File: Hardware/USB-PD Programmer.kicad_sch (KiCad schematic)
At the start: 22 parts, among them J1 Conn_01x08_Male, J2 Conn_01x04_Male, J3 Conn_01x02_Male, J4 Conn_01x02_Male, J5 Conn_01x02_Male, J6 Conn_01x02_Male, J7 Conn_01x07_Male, J9 QWIIC_Stackable, U1 R1501J033B-T1-JE, U2 CH340G, Y1 12M

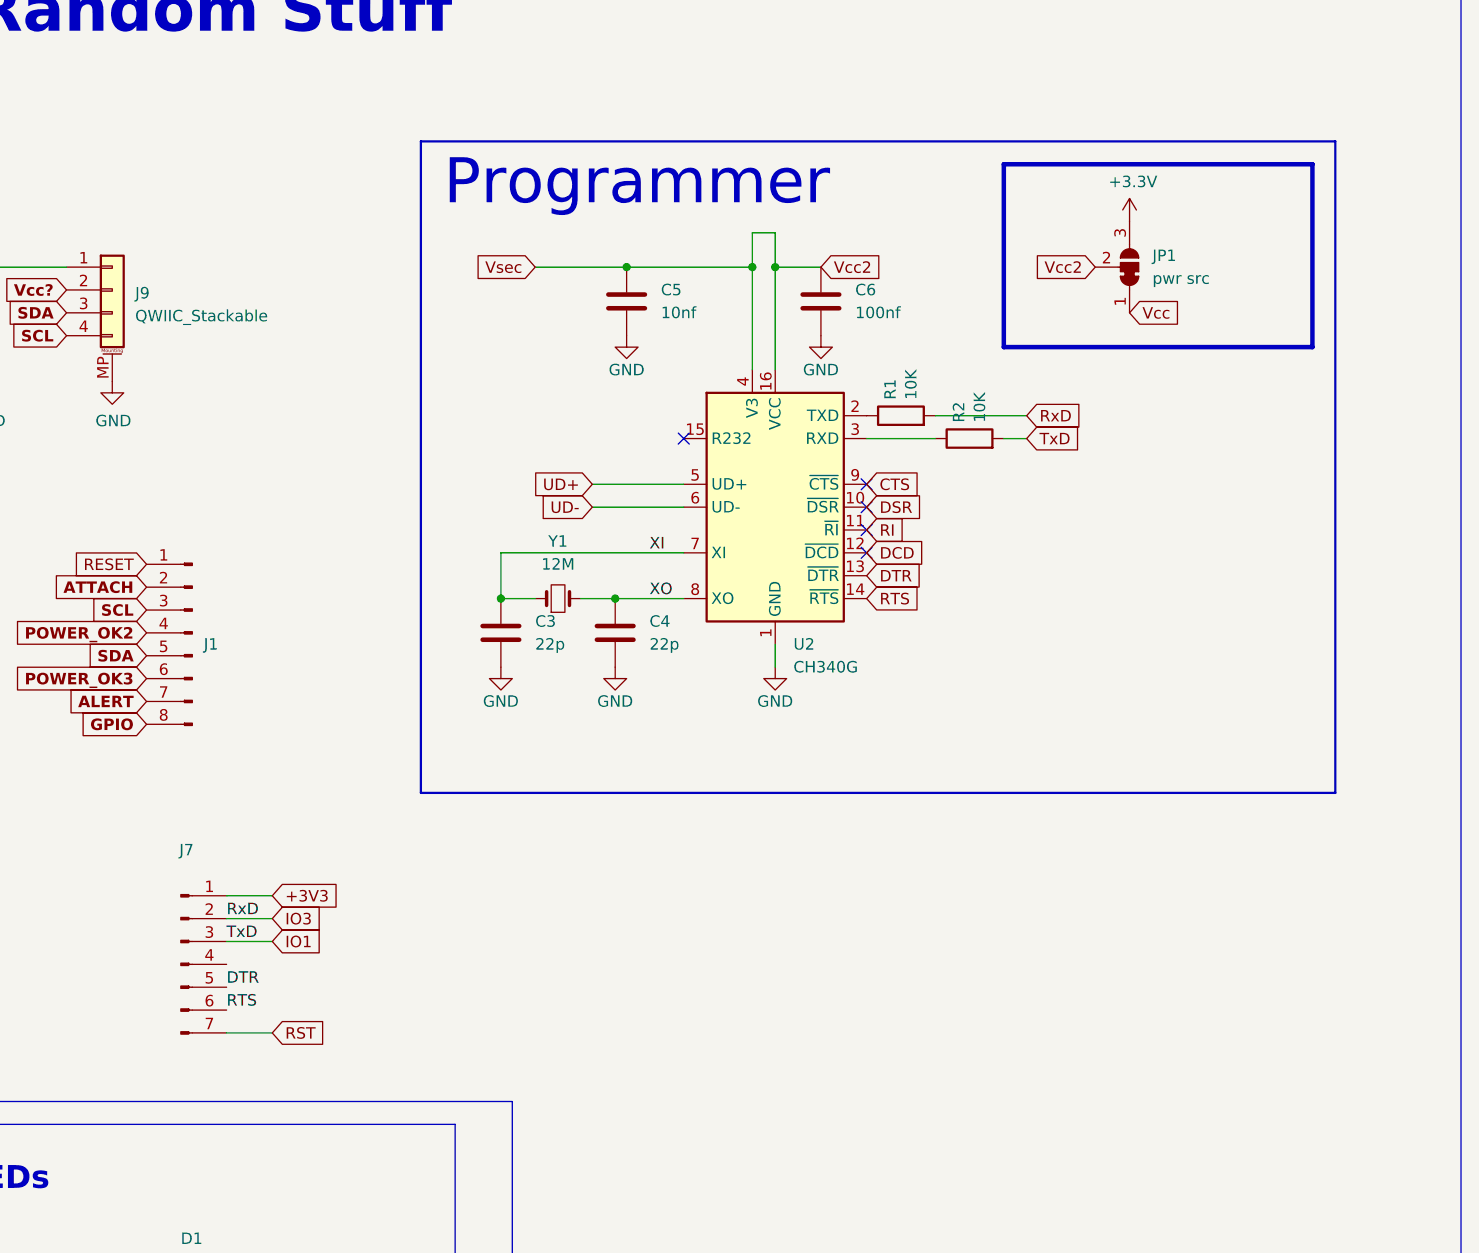
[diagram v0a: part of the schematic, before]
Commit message: Cleaned up design of the Programmer board
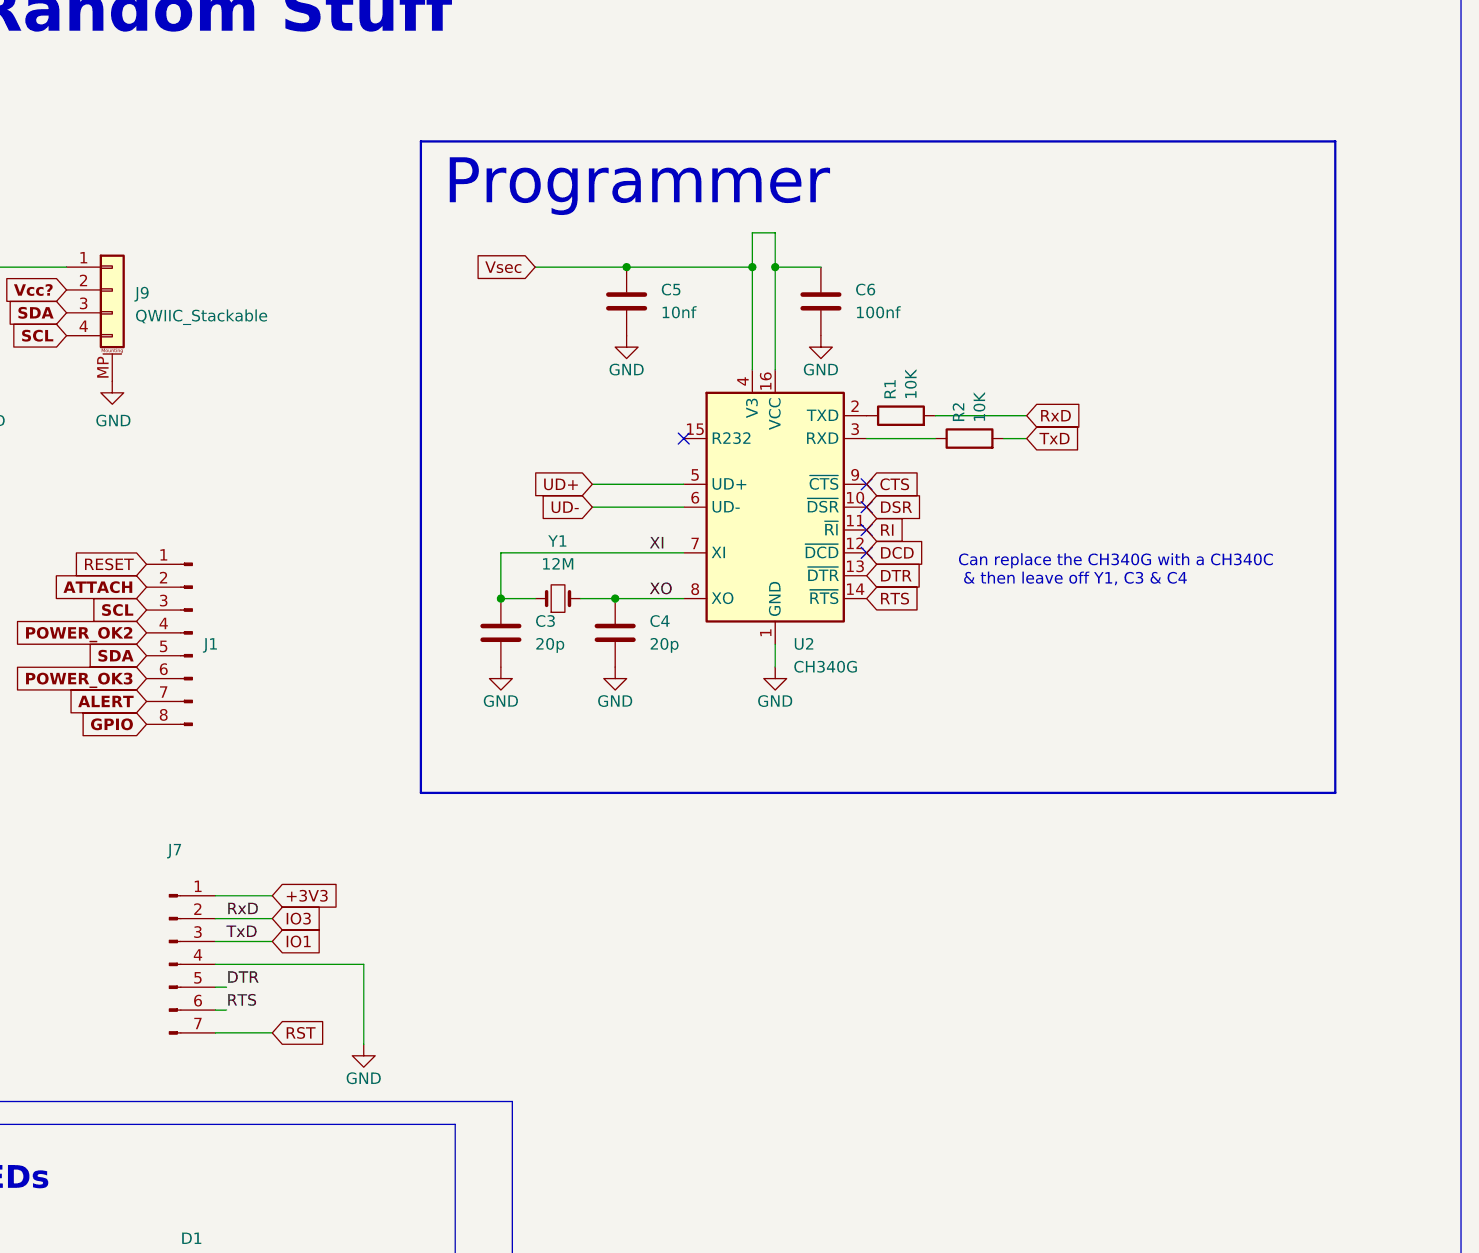
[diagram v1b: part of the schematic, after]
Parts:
- removed JP1: pwr src, Jumper:SolderJumper-3_P1.3mm_Bridged12_RoundedPad1.0x1.5mm_NumberLabels, symbol Jumper:SolderJumper_3_Bridged12
- C3, C4: value 22p -> 20p; LCSC C408549 (20pf C325469) -> C325469
- D1: footprint Footprints:SOT-23 (both sides) -> Package_TO_SOT_SMD:SOT-23
- R1, R2: LCSC (none) -> C25804
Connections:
- net GND: now also J7.4 (Pin_4)
- net Vcc2 renamed Vsec
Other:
- note added: "Can replace the CH340G with a CH340C & then leave off Y1, C3 & C4"
- moved on the sheet: J7

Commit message: Documentation...
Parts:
- added JP1: SolderJumper_2_Open, Tinker:SolderJumper-2_P_Open_Rounded_skinny, symbol Jumper:SolderJumper_2_Open
- U2: value CH340G -> CH340G/C; LCSC C14267 -> C14267/C84681
- renumbered J7 to J1, J1 to J7
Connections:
- net +3V3: now also JP1.2 (B)
- net Vsec: now also JP1.1 (A)
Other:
- moved on the sheet: J1

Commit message: Tinkerin' + RESET & LED on Programmer...
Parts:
- added D2: XL-2012RGBC, Tinker:XL-2012RGBC, symbol Device:LED_RGAB
- added D3: MHT170RGBCT, Tinker:MHT170RGBCT, symbol Device:LED_RGBA
- added R4, R5: 10K, Resistor_SMD:R_0603_1608Metric_Pad0.98x0.95mm_HandSolder, symbol Device:R
- added SW1: SW_Push, Tinker:SW_Push_TS273014TP, symbol Switch:SW_Push
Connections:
- net +3V3: now also SW1.2
- net GND: now also R4.1, R5.1
- net IO1: now also D2.1 (RK), D3.1 (RK)
- net IO3: now also D2.2 (GK), D3.2 (GK)
- net RST: now also SW1.1
- new net: D3.4 (A), R5.2
- new net: D2.3 (A), R4.2
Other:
- note added: "Board-Board"
- note added: "Control"
- note added: "QWIIC"
- moved on the sheet: C1, C2, J2, J3, J4, J5, J6, J7, J9, JP1, U1

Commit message: Programmer Board Indicators!
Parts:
- added D4: red, LED_SMD:LED_0603_1608Metric, symbol Device:LED
- added D5: green, LED_SMD:LED_0603_1608Metric, symbol Device:LED
- added D6, D7: yellow, LED_SMD:LED_0603_1608Metric, symbol Device:LED
- added R6, R7, R8, R9: 1k, Resistor_SMD:R_0603_1608Metric, symbol Device:R_US
- D2, R4: now left out of the parts list
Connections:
- net DTR: now also D6.1 (K)
- net GND: now also R6.1, R7.1
- net IO1: now also D4.2 (A)
- net IO3: now also D5.2 (A)
- net RTS: now also D7.1 (K)
- net Vsec: now also R8.2, R9.2
- new net: D6.2 (A), R8.1
- new net: D4.1 (K), R6.2
- new net: D5.1 (K), R7.2
- new net: D7.2 (A), R9.1
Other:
- moved on the sheet: D1, R3

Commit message: possibly, maybe, finalised Programmer Board?
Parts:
- removed D1: LED_Dual_AAK, Package_TO_SOT_SMD:SOT-23, symbol Device:LED_Dual_AAK
- removed D2: XL-2012RGBC, Tinker:XL-2012RGBC, symbol Device:LED_RGAB
- removed D3: MHT170RGBCT, Tinker:MHT170RGBCT, symbol Device:LED_RGBA
- removed R3, R4, R5: 10K, Resistor_SMD:R_0603_1608Metric_Pad0.98x0.95mm_HandSolder, symbol Device:R
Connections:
- net +3V3: no longer SW1.2
- net Vsec: now also SW1.2
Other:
- note removed: "grn"
- note removed: "red"
- title: Prototype Board -> USB-PD Programmer
- moved on the sheet: SW1

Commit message: Rabbit OCD attack...
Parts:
- added D1: blue, LED_SMD:LED_0603_1608Metric, symbol Device:LED
- added R1: 1k, Resistor_SMD:R_0603_1608Metric, symbol Device:R_US
- renumbered D4 to D2, D5 to D3, D6 to D4, D7 to D5, R6 to R2, R7 to R3, R8 to R4, R9 to R5, R1 to R6, R2 to R7
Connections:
- net +3V3: now also D1.2 (A)
- net GND: now also R1.1
- new net: D1.1 (K), R1.2
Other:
- note added: "ESP Programmer"
- note removed: "Random Stuff"
- moved on the sheet: C3, C4, C5, C6, D2, D3, D4, D5, J1, R2, R3, R4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

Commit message: Uber Rework!
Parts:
- J1: footprint Connector_PinHeader_2.54mm:PinHeader_1x07_P2.54mm_Vertical -> Tinker:Board_Stacker_7
- J2: footprint Tinker:PinHeader_1x04_P2.54mm_Vertical -> Tinker:Board_Stacker_4
- J3, J4, J5, J6: footprint Tinker:PinHeader_1x02_P2.54mm_Vertical -> Tinker:Board_Stacker_2
- renumbered D3 to D2, D2 to D3, R3 to R2, R2 to R3
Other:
- moved on the sheet: D2, D3, R2, R3
